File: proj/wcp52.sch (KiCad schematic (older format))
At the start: 0 parts

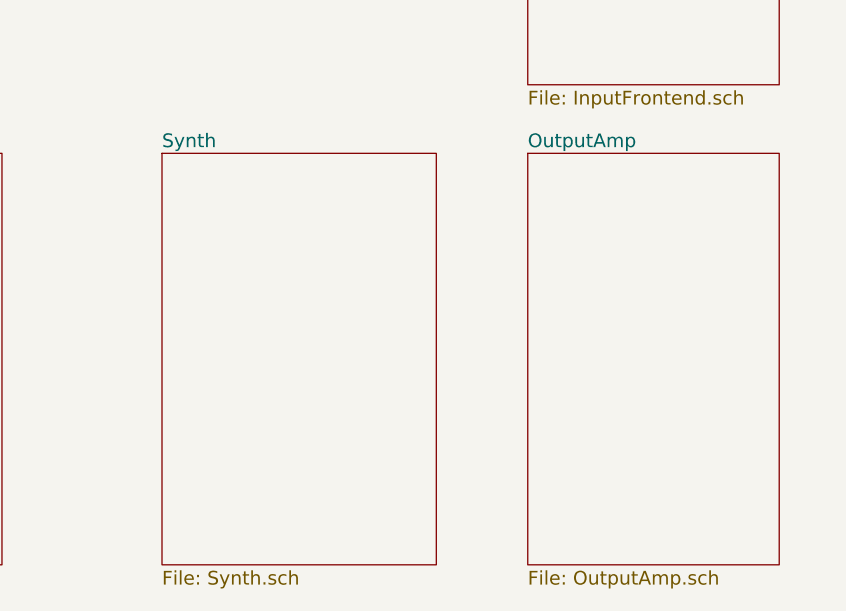
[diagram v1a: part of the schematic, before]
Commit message: Add output amplifier schematic
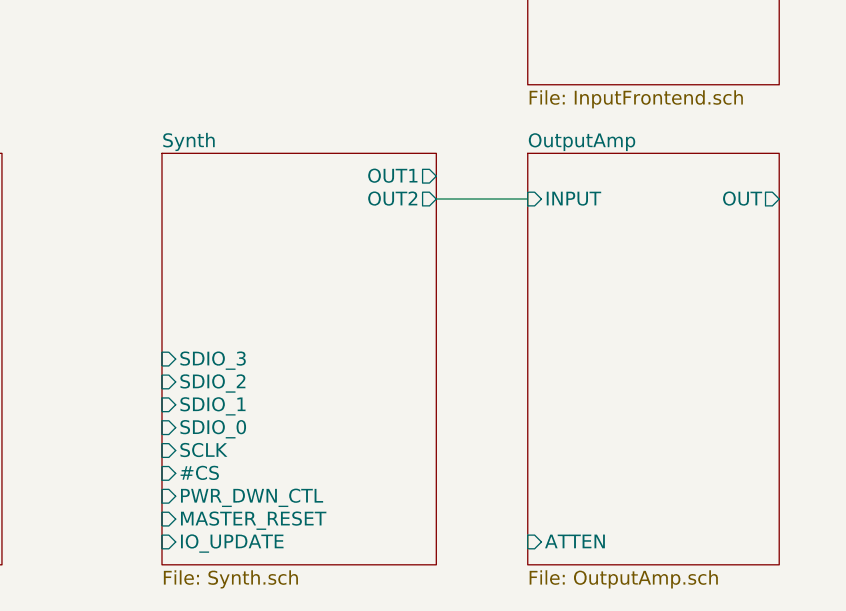
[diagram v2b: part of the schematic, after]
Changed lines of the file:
@@
 $Descr USLegal 14000 8500
 encoding utf-8
-Sheet 1 7
+Sheet 1 8
 Title "Block Diagram"
 Date "2015-02-28"
@@
 F0 "Synth" 60
 F1 "Synth.sch" 60
+F2 "IO_UPDATE" I L 9000 5700 60
+F3 "MASTER_RESET" I L 9000 5600 60
+F4 "PWR_DWN_CTL" I L 9000 5500 60
+F5 "#CS" I L 9000 5400 60
+F6 "SCLK" I L 9000 5300 60
+F7 "SDIO_0" I L 9000 5200 60
+F8 "SDIO_1" I L 9000 5100 60
+F9 "SDIO_2" I L 9000 5000 60
+F10 "SDIO_3" I L 9000 4900 60
+F11 "OUT1" O R 10200 4100 60
+F12 "OUT2" O R 10200 4200 60
 $EndSheet
 $Sheet
@@
 F0 "OutputAmp" 60
 F1 "OutputAmp.sch" 60
+F2 "INPUT" I L 10600 4200 60
+F3 "OUT" O R 11700 4200 60
+F4 "ATTEN" I L 10600 5700 60
 $EndSheet
 $Sheet
@@
 F1 "InputFrontend.sch" 60
 $EndSheet
+Wire Wire Line
+	10200 4200 10600 4200
 $EndSCHEMATC

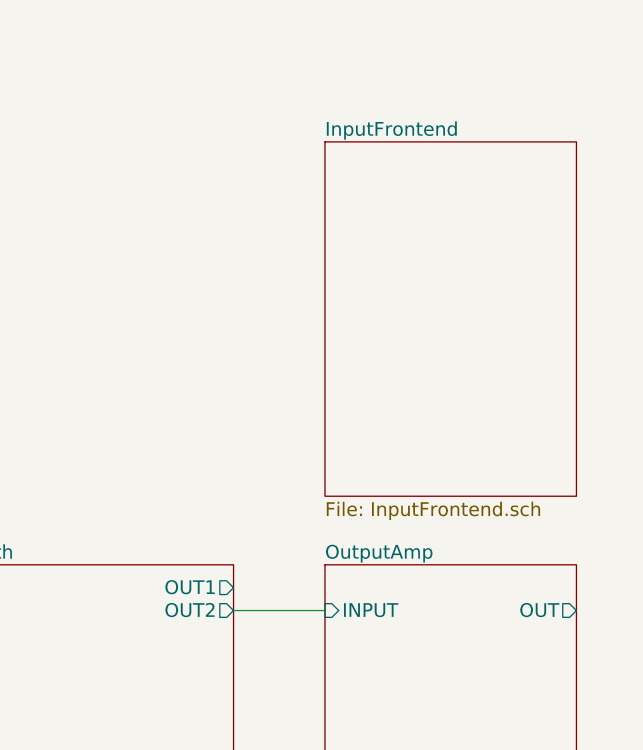
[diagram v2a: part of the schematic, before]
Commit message: Add frontend
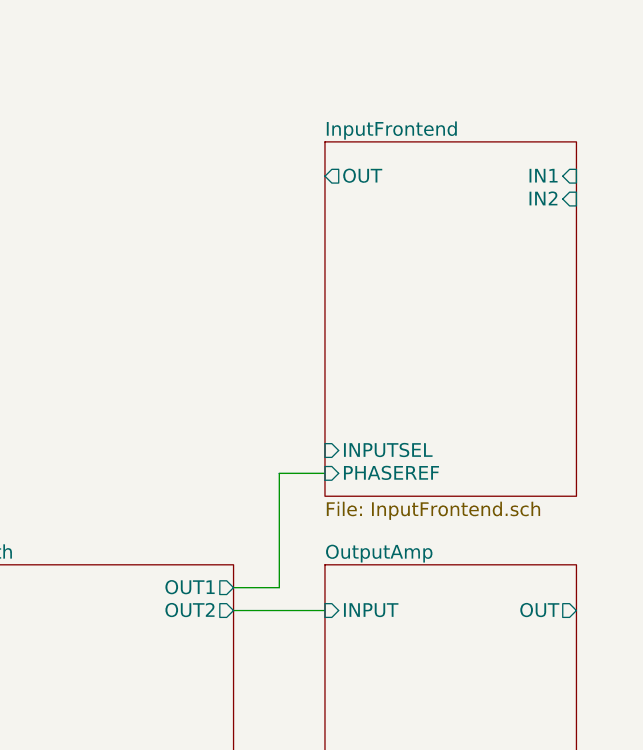
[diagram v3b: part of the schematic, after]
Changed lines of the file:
@@
 $Descr USLegal 14000 8500
 encoding utf-8
-Sheet 1 8
+Sheet 1 12
 Title "Block Diagram"
 Date "2015-02-28"
@@
 F0 "InputFrontend" 60
 F1 "InputFrontend.sch" 60
+F2 "OUT" O L 10600 2300 60
+F3 "IN1" I R 11700 2300 60
+F4 "IN2" I R 11700 2400 60
+F5 "INPUTSEL" I L 10600 3500 60
+F6 "PHASEREF" I L 10600 3600 60
 $EndSheet
 Wire Wire Line
 	10200 4200 10600 4200
+Wire Wire Line
+	10600 3600 10400 3600
+Wire Wire Line
+	10400 3600 10400 4100
+Wire Wire Line
+	10400 4100 10200 4100
 $EndSCHEMATC

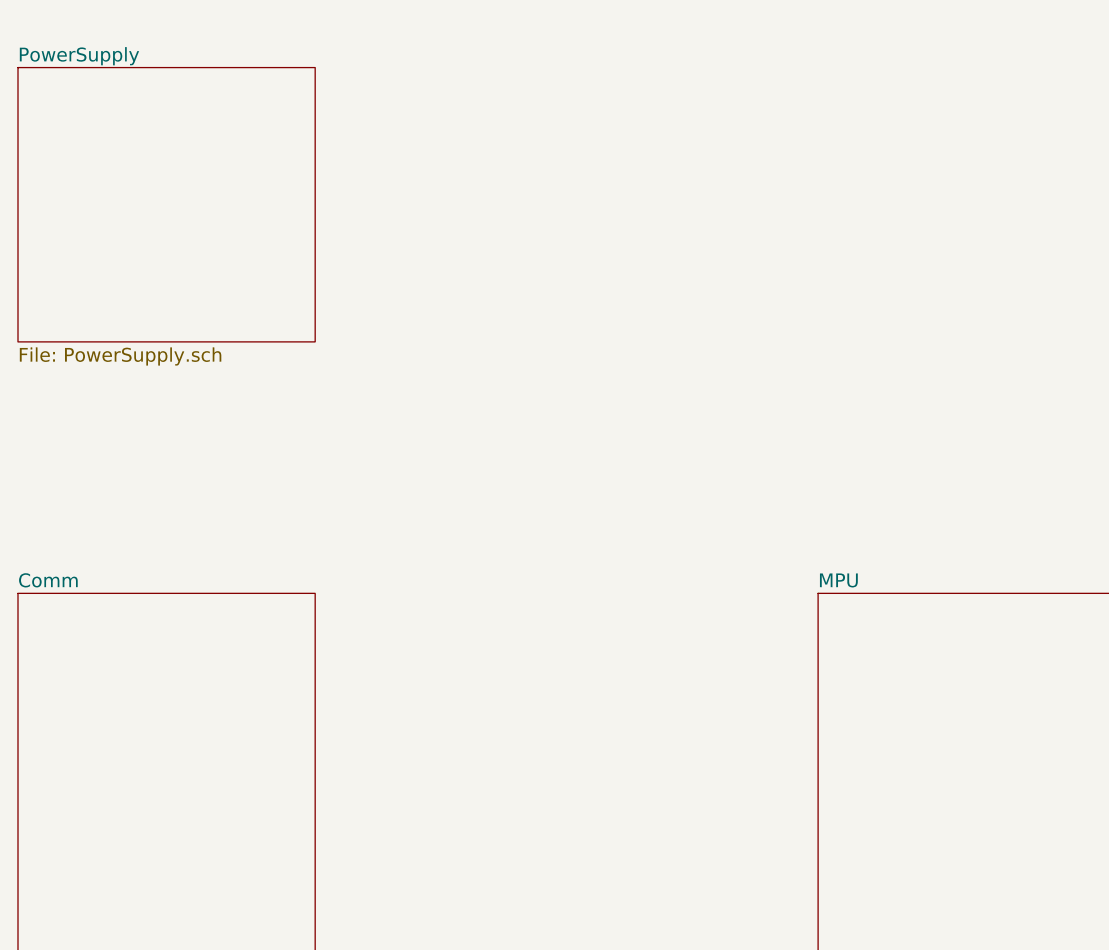
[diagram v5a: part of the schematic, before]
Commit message: Finish USB subcircuit
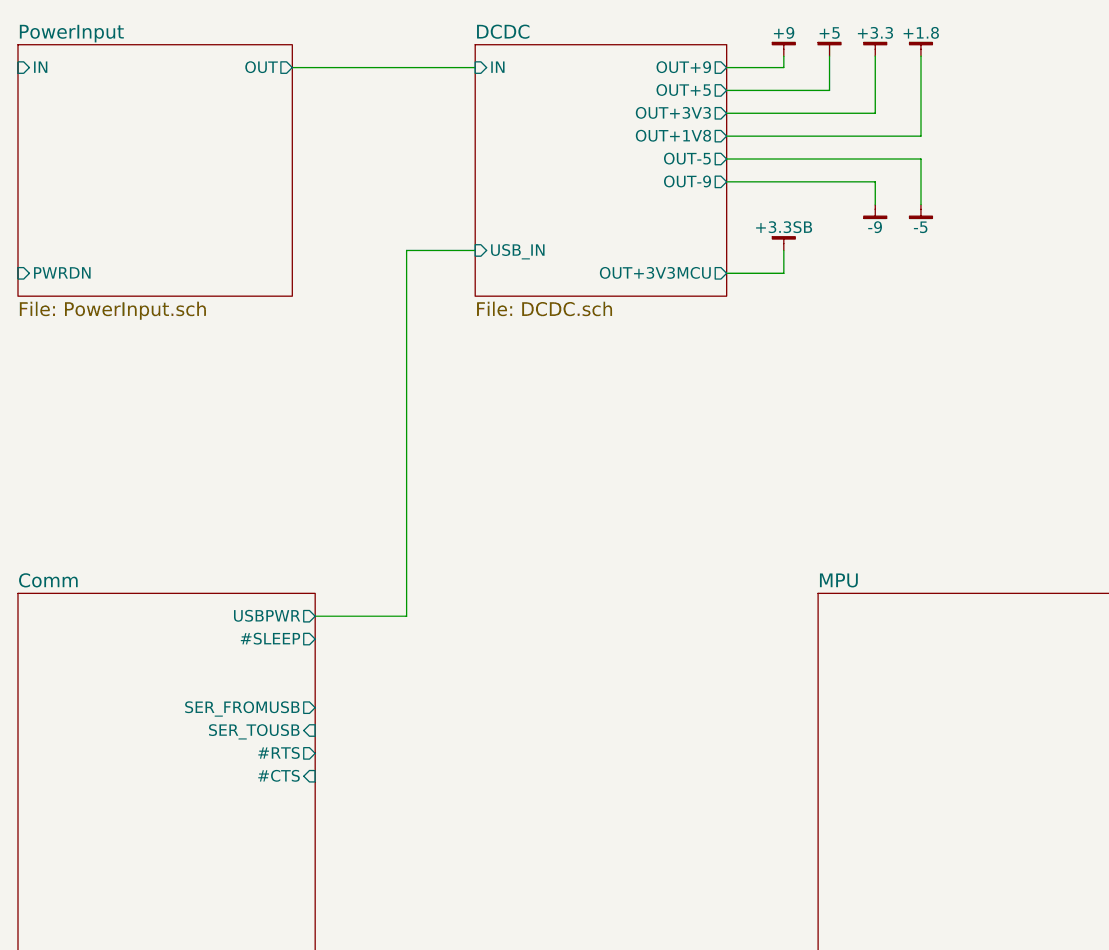
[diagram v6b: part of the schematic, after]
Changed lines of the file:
@@
 $Descr USLegal 14000 8500
 encoding utf-8
-Sheet 1 14
+Sheet 1 13
 Title "Block Diagram"
 Date "2015-02-28"
@@
 $EndDescr
 $Sheet
-S 1900 1700 1300 1200
-U 54F1FAAC
-F0 "PowerSupply" 60
-F1 "PowerSupply.sch" 60
-$EndSheet
-$Sheet
 S 5400 4000 2900 1800
 U 54F1FAC6
@@
 F0 "Comm" 60
 F1 "Comm.sch" 60
+F2 "SER_FROMUSB" O R 3200 4500 50
+F3 "SER_TOUSB" I R 3200 4600 50
+F4 "#RTS" O R 3200 4700 50
+F5 "#CTS" I R 3200 4800 50
+F6 "#SLEEP" O R 3200 4200 50
+F7 "USBPWR" O R 3200 4100 50
 $EndSheet
 $Sheet
@@
 Wire Wire Line
 	10400 4100 10200 4100
+$Sheet
+S 1900 1600 1200 1100
+U 54F49966
+F0 "PowerInput" 60
+F1 "PowerInput.sch" 60
+F2 "OUT" O R 3100 1700 50
+F3 "IN" I L 1900 1700 50
+F4 "PWRDN" I L 1900 2600 50
+$EndSheet
+$Sheet
+S 3900 1600 1100 1100
+U 54F4F7B6
+F0 "DCDC" 60
+F1 "DCDC.sch" 60
+F2 "OUT-9" O R 5000 2200 50
+F3 "IN" I L 3900 1700 50
+F4 "OUT+3V3" O R 5000 1900 50
+F5 "OUT+9" O R 5000 1700 50
+F6 "OUT+5" O R 5000 1800 50
+F7 "OUT-5" O R 5000 2100 50
+F8 "OUT+1V8" O R 5000 2000 50
+F9 "USB_IN" I L 3900 2500 50
+F10 "OUT+3V3MCU" O R 5000 2600 50
+$EndSheet
+Wire Wire Line
+	3100 1700 3900 1700
+$Comp
+L +9 #PWR?
+U 1 1 54F69DB4
+P 5250 1650
+F 0 "#PWR?" H 5250 1700 30  0001 C CNN
+F 1 "+9" H 5250 1750 50  0000 C CNN
+F 2 "" H 5250 1650 60  0000 C CNN
+F 3 "" H 5250 1650 60  0000 C CNN
+	1    5250 1650
+	1    0    0    -1
+$EndComp
+Wire Wire Line
+	5000 1700 5250 1700
+Wire Wire Line
+	5250 1700 5250 1650
+$Comp
+L +5 #PWR?
+U 1 1 54F69DBC
+P 5450 1650
+F 0 "#PWR?" H 5450 1700 30  0001 C CNN
+F 1 "+5" H 5450 1750 50  0000 C CNN
+F 2 "" H 5450 1650 60  0000 C CNN
+F 3 "" H 5450 1650 60  0000 C CNN
+	1    5450 1650
+	1    0    0    -1
+$EndComp
+Wire Wire Line
+	5450 1650 5450 1800
+Wire Wire Line
+	5450 1800 5000 1800
+$Comp
+L +3.3 #PWR?
+U 1 1 54F69DC4
+P 5650 1650
+F 0 "#PWR?" H 5650 1700 30  0001 C CNN
+F 1 "+3.3" H 5650 1750 50  0000 C CNN
+F 2 "" H 5650 1650 60  0000 C CNN
+F 3 "" H 5650 1650 60  0000 C CNN
+	1    5650 1650
+	1    0    0    -1
+$EndComp
+Wire Wire Line
+	5650 1650 5650 1900
+Wire Wire Line
+	5650 1900 5000 1900
+$Comp
+L +1.8 #PWR?
+U 1 1 54F69DCC
+P 5850 1650
+F 0 "#PWR?" H 5850 1700 30  0001 C CNN
+F 1 "+1.8" H 5850 1750 50  0000 C CNN
+F 2 "" H 5850 1650 60  0000 C CNN
+F 3 "" H 5850 1650 60  0000 C CNN
+	1    5850 1650
+	1    0    0    -1
+$EndComp
+Wire Wire Line
+	5850 1650 5850 2000
+Wire Wire Line
+	5850 2000 5000 2000
+$Comp
+L -5 #PWR?
+U 1 1 54F69DD4
+P 5850 2300
+F 0 "#PWR?" H 5850 2250 30  0001 C CNN
+F 1 "-5" H 5850 2200 50  0000 C CNN
+F 2 "" H 5850 2300 60  0000 C CNN
+F 3 "" H 5850 2300 60  0000 C CNN
+	1    5850 2300
+	1    0    0    -1
+$EndComp
+Wire Wire Line
+	5850 2300 5850 2100
+Wire Wire Line
+	5850 2100 5000 2100
+$Comp
+L -9 #PWR?
+U 1 1 54F69DDC
+P 5650 2300
+F 0 "#PWR?" H 5650 2250 30  0001 C CNN
+F 1 "-9" H 5650 2200 50  0000 C CNN
+F 2 "" H 5650 2300 60  0000 C CNN
+F 3 "" H 5650 2300 60  0000 C CNN
+	1    5650 2300
+	1    0    0    -1
+$EndComp
+Wire Wire Line
+	5650 2300 5650 2200
+Wire Wire Line
+	5650 2200 5000 2200
+$Comp
+L +3.3SB #PWR?
+U 1 1 54F69DE4
+P 5250 2500
+F 0 "#PWR?" H 5250 2550 30  0001 C CNN
+F 1 "+3.3SB" H 5250 2600 50  0000 C CNN
+F 2 "" H 5250 2500 60  0000 C CNN
+F 3 "" H 5250 2500 60  0000 C CNN
+	1    5250 2500
+	1    0    0    -1
+$EndComp
+Wire Wire Line
+	5250 2500 5250 2600
+Wire Wire Line
+	5250 2600 5000 2600
+Wire Wire Line
+	3200 4100 3600 4100
+Wire Wire Line
+	3600 4100 3600 2500
+Wire Wire Line
+	3600 2500 3900 2500
 $EndSCHEMATC

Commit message: PCB work, mostly mechanical
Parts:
- added J2: IN1, manuf:CONN-BNC-1-1337543-0, symbol CONN-BNC-1-1337543-0
- added J3: IN2, manuf:CONN-BNC-1-1337543-0, symbol CONN-BNC-1-1337543-0
- added J4: OUT, manuf:CONN-BNC-1-1337543-0, symbol CONN-BNC-1-1337543-0
- added J5: CONN-PJ-037A, conn-cui:CONN-PJ-037A, symbol CONN-PJ-037A
- added MP2, MP3, MP4, MP5: SCREW, mech:SCREW-3-SUPPORTED, symbol SCREW
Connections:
- net InputFrontend/IN1: now also J2.1
- net InputFrontend/IN2: now also J3.1
- net OutputAmp/OUT: now also J4.1
- net PowerInput/IN: now also J5.1
- new net GND: J2.2, J3.2, J4.2, J5.2, MP2.1, MP3.1, MP4.1, MP5.1
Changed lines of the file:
@@
 LIBS:Xilinx
 LIBS:pasv-xtal
+LIBS:conn-te
 LIBS:wcp52-cache
 EELAYER 25 0
@@
 Wire Wire Line
 	3600 2500 3900 2500
+$Comp
+L SCREW MP2
+U 1 1 54F6A5D4
+P 1000 7350
+F 0 "MP2" H 1000 7600 50  0000 C CNN
+F 1 "SCREW" H 1000 7500 50  0000 C CNN
+F 2 "mech:SCREW-3-SUPPORTED" H 1000 7350 50  0001 C CNN
+F 3 "" H 1000 7350 60  0000 C CNN
+	1    1000 7350
+	1    0    0    -1
+$EndComp
+$Comp
+L GND #PWR08
+U 1 1 54F6A6BD
+P 1000 7550
+F 0 "#PWR08" H 1000 7550 30  0001 C CNN
+F 1 "GND" H 1000 7480 30  0001 C CNN
+F 2 "" H 1000 7550 60  0000 C CNN
+F 3 "" H 1000 7550 60  0000 C CNN
+	1    1000 7550
+	1    0    0    -1
+$EndComp
+Wire Wire Line
+	1000 7550 1000 7500
+$Comp
+L SCREW MP3
+U 1 1 54F6A8B8
+P 1300 7350
+F 0 "MP3" H 1300 7600 50  0000 C CNN
+F 1 "SCREW" H 1300 7500 50  0000 C CNN
+F 2 "mech:SCREW-3-SUPPORTED" H 1300 7350 50  0001 C CNN
+F 3 "" H 1300 7350 60  0000 C CNN
+	1    1300 7350
+	1    0    0    -1
+$EndComp
+$Comp
+L GND #PWR09
+U 1 1 54F6A8BE
+P 1300 7550
+F 0 "#PWR09" H 1300 7550 30  0001 C CNN
+F 1 "GND" H 1300 7480 30  0001 C CNN
+F 2 "" H 1300 7550 60  0000 C CNN
+F 3 "" H 1300 7550 60  0000 C CNN
+	1    1300 7550
+	1    0    0    -1
+$EndComp
+Wire Wire Line
+	1300 7550 1300 7500
+$Comp
+L SCREW MP4
+U 1 1 54F6A9EF
+P 1600 7350
+F 0 "MP4" H 1600 7600 50  0000 C CNN
+F 1 "SCREW" H 1600 7500 50  0000 C CNN
+F 2 "mech:SCREW-3-SUPPORTED" H 1600 7350 50  0001 C CNN
+F 3 "" H 1600 7350 60  0000 C CNN
+	1    1600 7350
+	1    0    0    -1
+$EndComp
+$Comp
+L GND #PWR010
+U 1 1 54F6A9F5
+P 1600 7550
+F 0 "#PWR010" H 1600 7550 30  0001 C CNN
+F 1 "GND" H 1600 7480 30  0001 C CNN
+F 2 "" H 1600 7550 60  0000 C CNN
+F 3 "" H 1600 7550 60  0000 C CNN
+	1    1600 7550
+	1    0    0    -1
+$EndComp
+Wire Wire Line
+	1600 7550 1600 7500
+$Comp
+L SCREW MP5
+U 1 1 54F6A9FC
+P 1900 7350
+F 0 "MP5" H 1900 7600 50  0000 C CNN
+F 1 "SCREW" H 1900 7500 50  0000 C CNN
+F 2 "mech:SCREW-3-SUPPORTED" H 1900 7350 50  0001 C CNN
+F 3 "" H 1900 7350 60  0000 C CNN
+	1    1900 7350
+	1    0    0    -1
+$EndComp
+$Comp
+L GND #PWR011
+U 1 1 54F6AA02
+P 1900 7550
+F 0 "#PWR011" H 1900 7550 30  0001 C CNN
+F 1 "GND" H 1900 7480 30  0001 C CNN
+F 2 "" H 1900 7550 60  0000 C CNN
+F 3 "" H 1900 7550 60  0000 C CNN
+	1    1900 7550
+	1    0    0    -1
+$EndComp
+Wire Wire Line
+	1900 7550 1900 7500
+$Comp
+L CONN-BNC-1-1337543-0 J2
+U 1 1 54F6DB05
+P 12800 2300
+F 0 "J2" H 12800 2500 50  0000 C CNN
+F 1 "IN1" H 12800 2400 50  0000 C CNN
+F 2 "manuf:CONN-BNC-1-1337543-0" H 12800 2300 50  0001 C CNN
+F 3 "" H 12800 2300 50  0000 C CNN
+	1    12800 2300
+	-1   0    0    -1
+$EndComp
+Wire Wire Line
+	12700 2300 11700 2300
+$Comp
+L GND #PWR012
+U 1 1 54F6DEB9
+P 12800 2450
+F 0 "#PWR012" H 12800 2450 30  0001 C CNN
+F 1 "GND" H 12800 2380 30  0001 C CNN
+F 2 "" H 12800 2450 60  0000 C CNN
+F 3 "" H 12800 2450 60  0000 C CNN
+	1    12800 2450
+	1    0    0    -1
+$EndComp
+Wire Wire Line
+	12800 2450 12800 2400
+$Comp
+L CONN-BNC-1-1337543-0 J3
+U 1 1 54F6DFD5
+P 12800 2800
+F 0 "J3" H 12800 3000 50  0000 C CNN
+F 1 "IN2" H 12800 2900 50  0000 C CNN
+F 2 "manuf:CONN-BNC-1-1337543-0" H 12800 2800 50  0001 C CNN
+F 3 "" H 12800 2800 50  0000 C CNN
+	1    12800 2800
+	-1   0    0    -1
+$EndComp
+Wire Wire Line
+	12700 2800 12400 2800
+Wire Wire Line
+	12400 2800 12400 2400
+Wire Wire Line
+	12400 2400 11700 2400
+$Comp
+L GND #PWR013
+U 1 1 54F6E211
+P 12800 2950
+F 0 "#PWR013" H 12800 2950 30  0001 C CNN
+F 1 "GND" H 12800 2880 30  0001 C CNN
+F 2 "" H 12800 2950 60  0000 C CNN
+F 3 "" H 12800 2950 60  0000 C CNN
+	1    12800 2950
+	1    0    0    -1
+$EndComp
+Wire Wire Line
+	12800 2900 12800 2950
+$Comp
+L CONN-BNC-1-1337543-0 J4
+U 1 1 54F6E521
+P 12800 4200
+F 0 "J4" H 12800 4400 50  0000 C CNN
+F 1 "OUT" H 12800 4300 50  0000 C CNN
+F 2 "manuf:CONN-BNC-1-1337543-0" H 12800 4200 50  0001 C CNN
+F 3 "" H 12800 4200 50  0000 C CNN
+	1    12800 4200
+	-1   0    0    -1
+$EndComp
+Wire Wire Line
+	12700 4200 11700 4200
+$Comp
+L GND #PWR014
+U 1 1 54F6E686
+P 12800 4350
+F 0 "#PWR014" H 12800 4350 30  0001 C CNN
+F 1 "GND" H 12800 4280 30  0001 C CNN
+F 2 "" H 12800 4350 60  0000 C CNN
+F 3 "" H 12800 4350 60  0000 C CNN
+	1    12800 4350
+	1    0    0    -1
+$EndComp
+Wire Wire Line
+	12800 4300 12800 4350
+$Comp
+L CONN-PJ-037A J5
+U 1 1 54F71BBD
+P 1300 1700
+F 0 "J5" H 1300 1950 50  0000 C CNN
+F 1 "CONN-PJ-037A" H 1300 1850 50  0000 C CNN
+F 2 "conn-cui:CONN-PJ-037A" H 1300 1700 50  0001 C CNN
+F 3 "" H 1400 1700 60  0000 C CNN
+	1    1300 1700
+	-1   0    0    -1
+$EndComp
+Wire Wire Line
+	1500 1700 1900 1700
+$Comp
+L GND #PWR015
+U 1 1 54F71DCD
+P 1200 1950
+F 0 "#PWR015" H 1200 1950 30  0001 C CNN
+F 1 "GND" H 1200 1880 30  0001 C CNN
+F 2 "" H 1200 1950 60  0000 C CNN
+F 3 "" H 1200 1950 60  0000 C CNN
+	1    1200 1950
+	1    0    0    -1
+$EndComp
+Wire Wire Line
+	1200 1950 1200 1900
 $EndSCHEMATC
